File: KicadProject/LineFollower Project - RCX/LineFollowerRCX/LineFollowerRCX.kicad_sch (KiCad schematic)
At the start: 13 parts, among them J1 Conn_01x11_Pin, J10 GND pinos, J2 Motor 1, J3 Motor 1, J4 Modulo bluetooth, J6 Sensor Lateral - Direita, J8 Conector sensor lateral Direi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, J9 VCC pinos, U1 ROB-14450, U2 LM7805_TO220

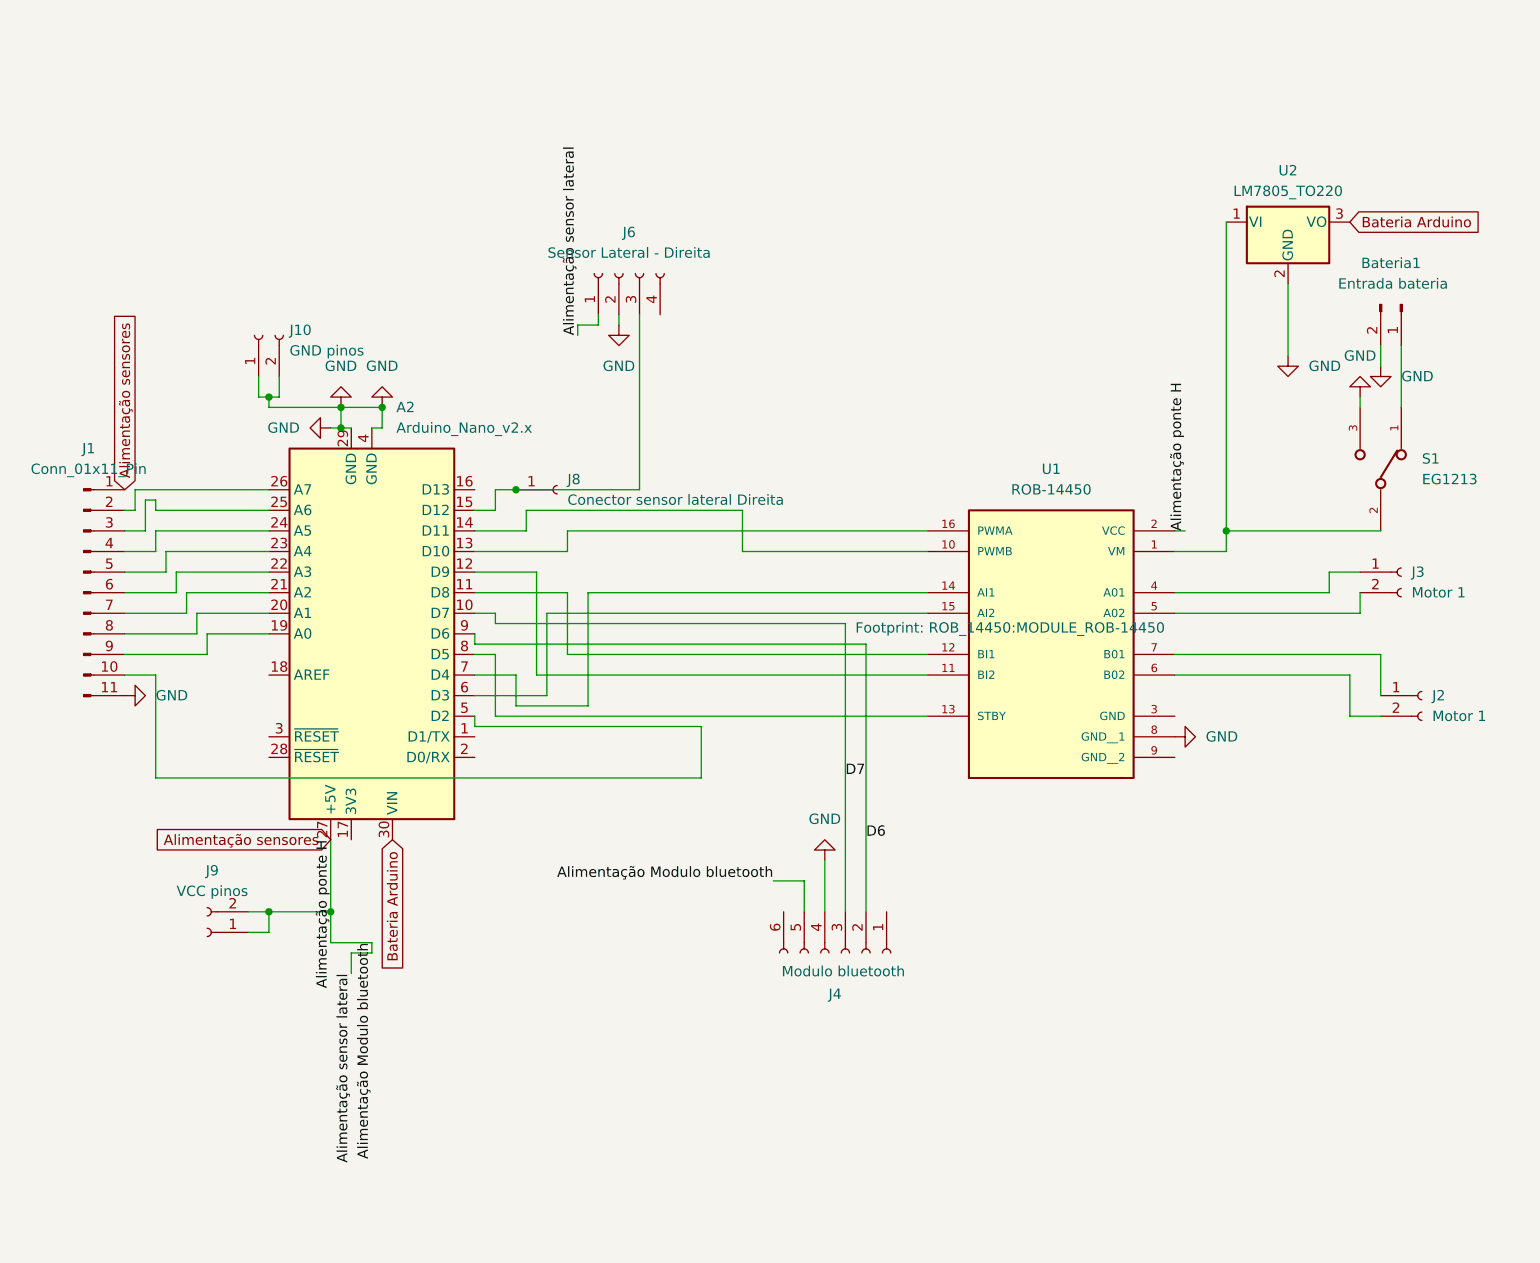
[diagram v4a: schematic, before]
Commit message: fix: ajusta pinos de alimentacao da ponte h e sensores
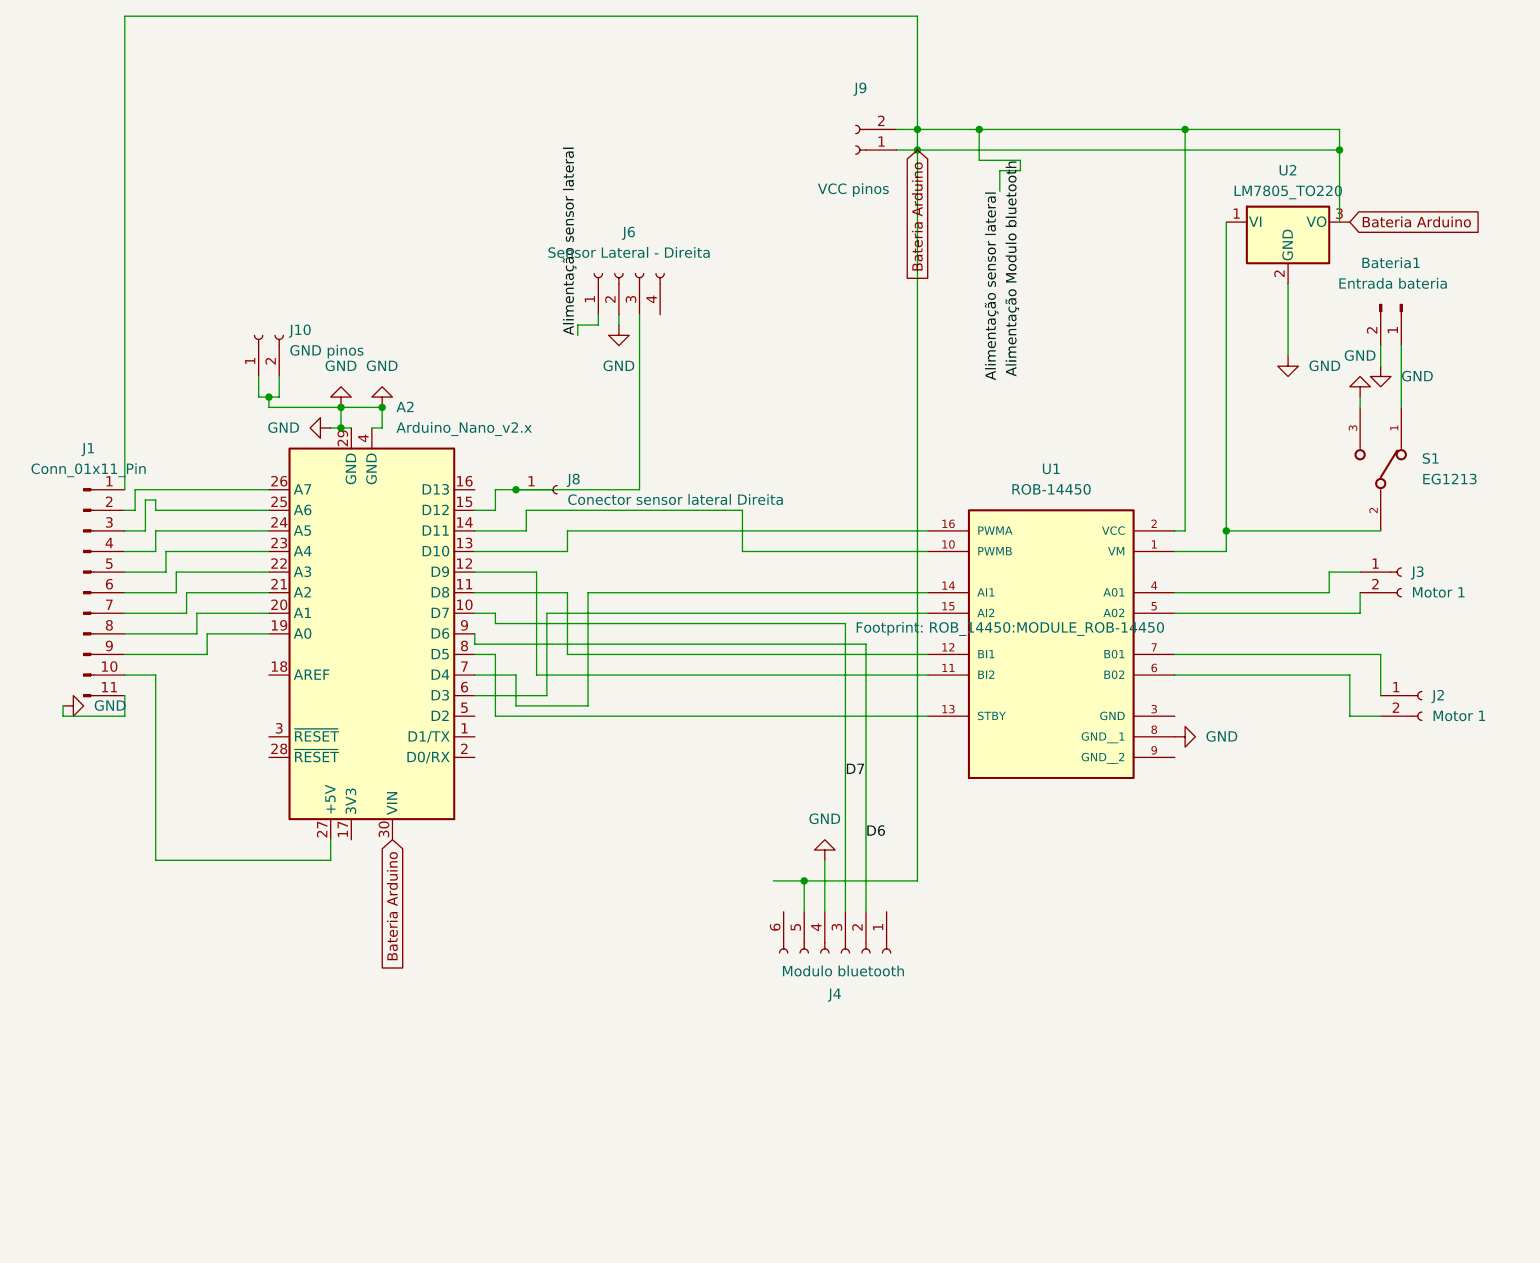
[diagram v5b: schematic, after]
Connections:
- net Bateria Arduino: now also J1.1 (Pin_1), J4.5 (VCC), J6.1 (VCC), J9.1 (Pin_1), J9.2 (Pin_2), U1.2 (VCC)
- net at J1.10 (Pin_10): now also A2.27 (+5V); no longer A2.5 (D2)
- removed net Alimentação sensores: A2.27 (+5V), J1.1 (Pin_1), J4.5 (VCC), J6.1 (VCC), J9.1 (Pin_1), J9.2 (Pin_2), U1.2 (VCC)
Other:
- moved on the sheet: J9
